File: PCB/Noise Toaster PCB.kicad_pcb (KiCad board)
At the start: 2 copper layers, 132.1 x 68.6 mm, 140 parts, among them Q1 2N5457, Q10 2N3906, Q2 2N3904, Q3 2N3904, Q4 2N3904, Q5 2N3904, Q6 2N3904, Q7 2N5457, Q8 2N5457, Q9 2N5457, U1 LM324, U2 LM324, U3 LM386

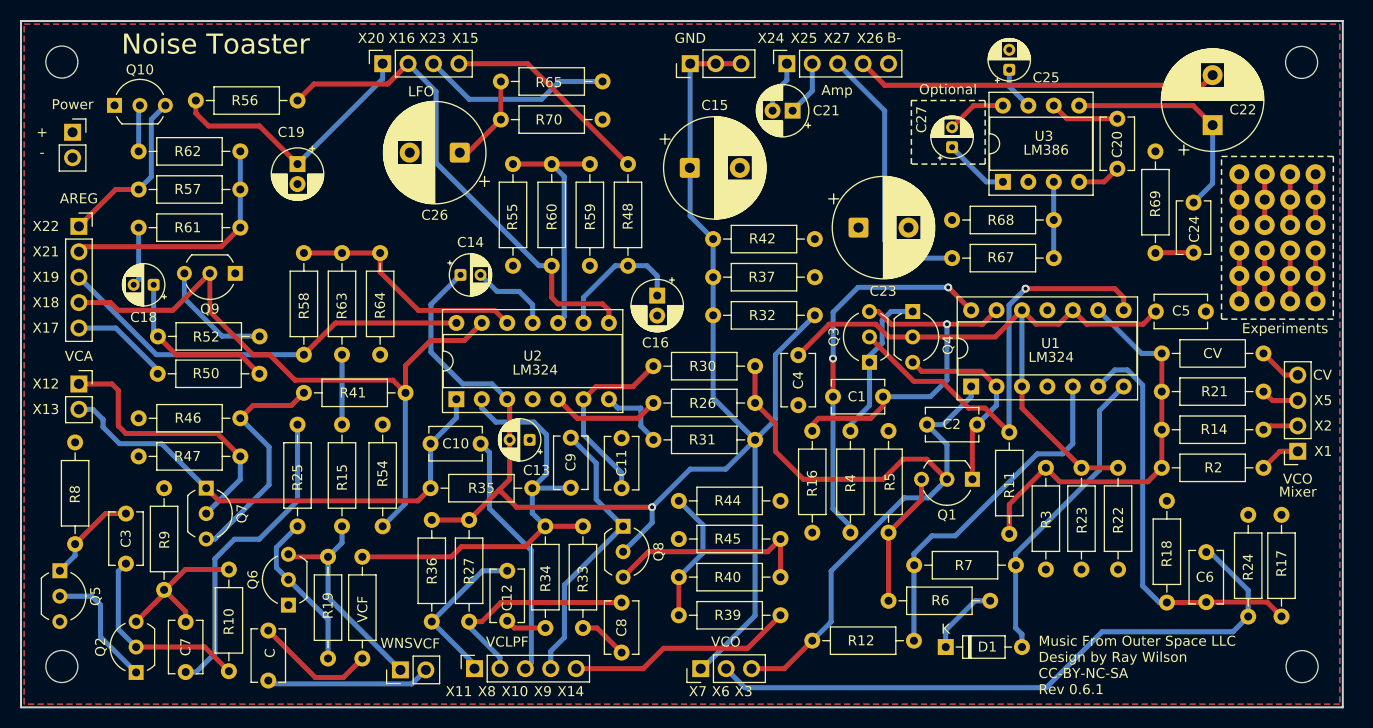
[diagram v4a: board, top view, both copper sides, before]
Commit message: Move footprints to allow mininum 20 mils distance between courtyards
except for the Q3 Q4 transistor pair
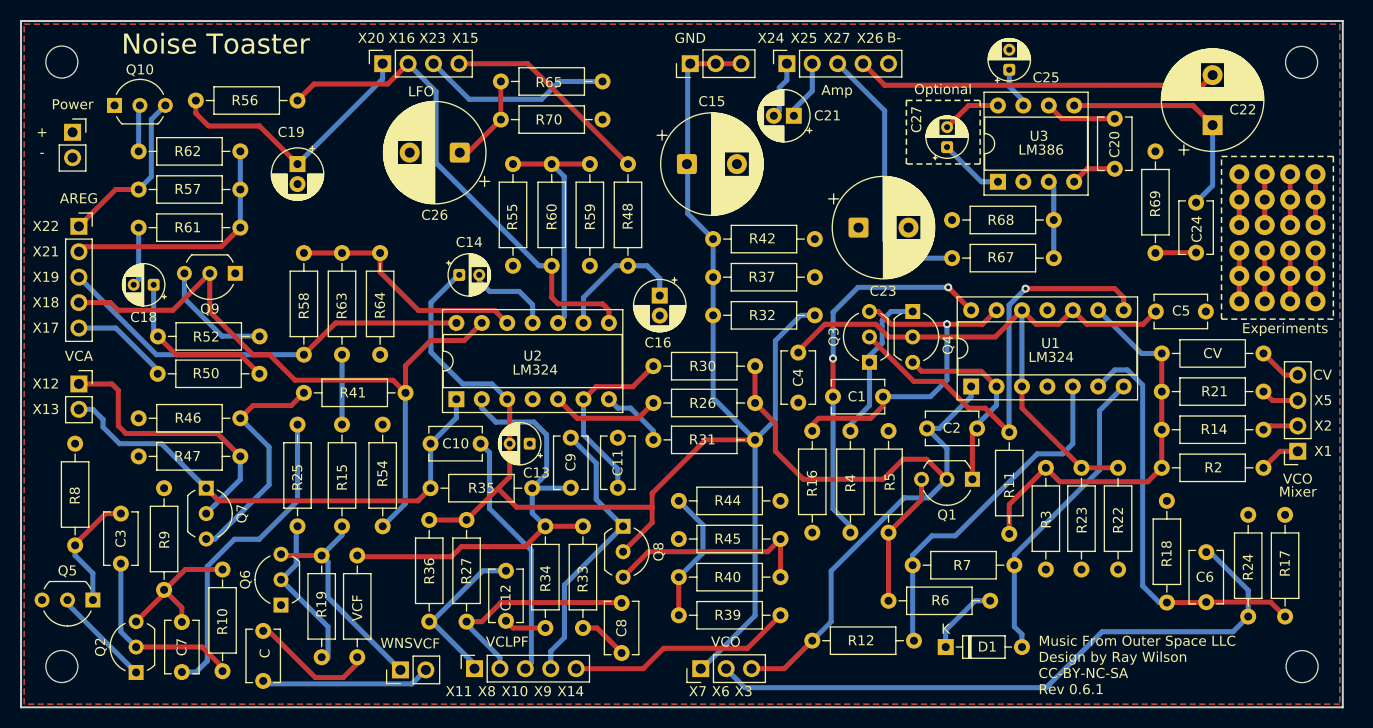
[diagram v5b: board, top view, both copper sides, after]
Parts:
- moved Q5 4.41 mm to (82.5, 133.1), turned to 180 degrees
- moved Q6 0.74 mm to (101.2, 133.6)
- moved R19 0.65 mm to (105.3, 128.7)
- moved R10 0.64 mm to (95.4, 130.1)
- moved C21 0.52 mm to (152.5, 84.7)
- moved VCF 0.52 mm to (108.9, 138.8)
- moved C 0.51 mm to (99.5, 136.2)
- moved C3 0.51 mm to (85.2, 124.5)
- moved C27 0.50 mm to (167.8, 87.9)
- moved U3 0.50 mm to (172.9, 91.3)
- moved C15 0.48 mm to (141.8, 89.6)
- moved C11 0.38 mm to (134.9, 116.9)
- moved C13 0.38 mm to (126.1, 117.5)
- moved C2 0.38 mm to (170.8, 116.0)
- moved C7 0.38 mm to (91.3, 135.3)
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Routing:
- net Net-(Q5-E): track 9.64 -> 12.0 mm
- net B-: track 31.2 -> 28.9 mm
- net GND: track 155.8 -> 157.4 mm, vias 1 -> 0
- net Net-(Q2-B): track 19.7 -> 18.4 mm
- net Net-(Q2-C): track 15.4 -> 14.6 mm
- net /WNS: track 21.6 -> 22.4 mm
- net Net-(U3-BYPASS): track 4.37 -> 3.66 mm
- net /Front Panel/X8: track 21.5 -> 22.1 mm
- net Net-(Q6-B): track 16.2 -> 15.7 mm

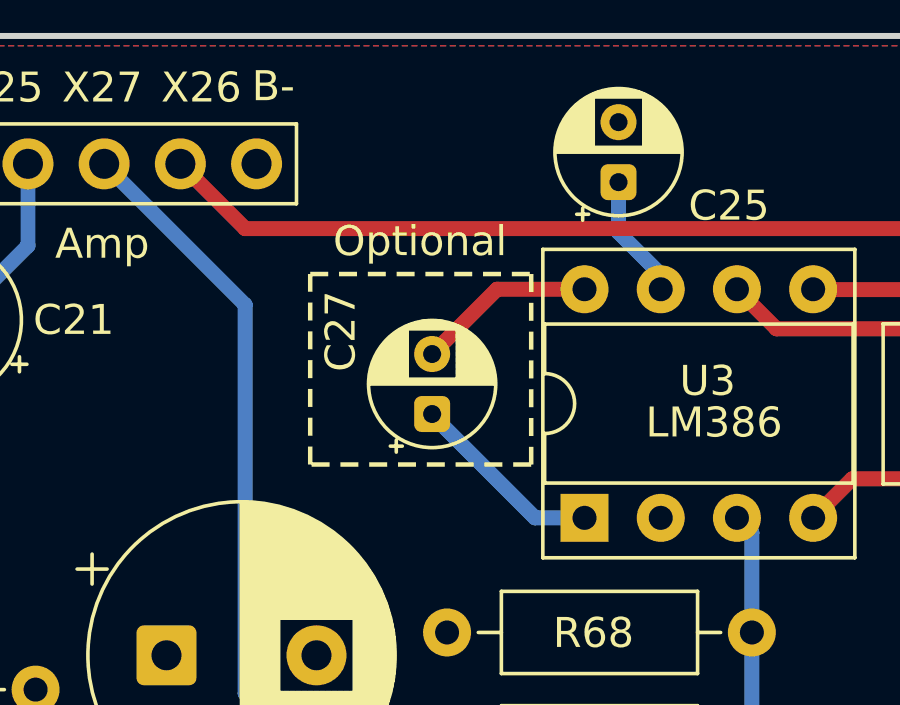
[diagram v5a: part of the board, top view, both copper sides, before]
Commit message: Added Holes for Gain Control
If you add the 10uF cap to the amplifier, you can control it by adding a potentiometer between it and pin 1
Following the internal gain equation, 30k/(150+R), you get 200 with no resistor and 20 with a 1350 ohm resistor
Choosing a 1k pot will leave you with a gain of 26 (28db) and a 1.5k equal to 18 gain (25db), albeit with some clipping
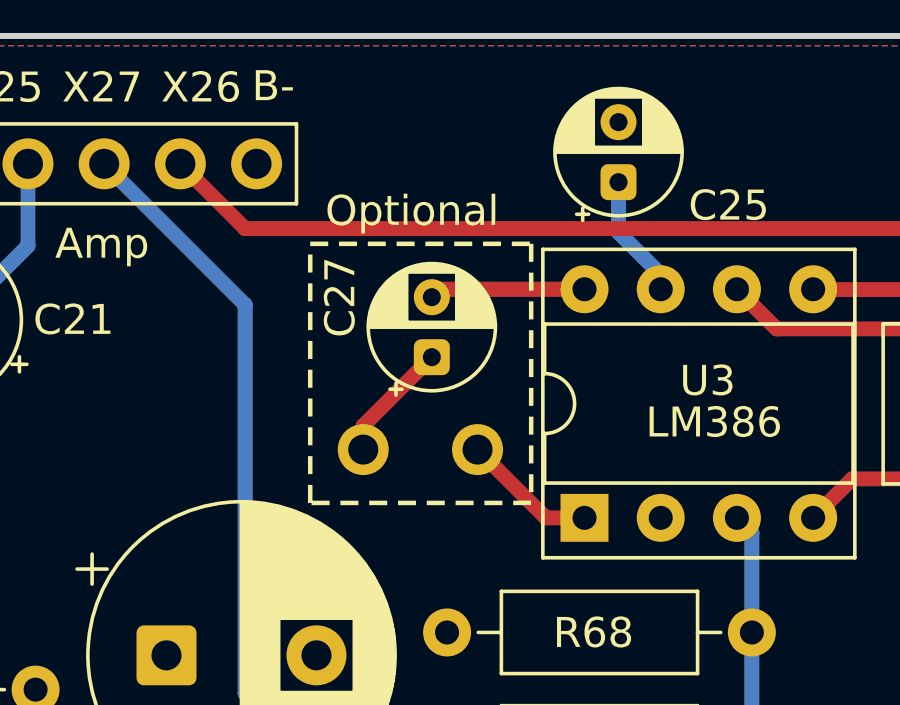
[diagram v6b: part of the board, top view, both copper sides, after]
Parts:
- added ?: , , F.Cu at (169.3, 89.1)
- added ?: , , F.Cu at (165.5, 89.1)
- moved C27 1.90 mm to (167.8, 86.0)
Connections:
- U3 pad 1: Net-(C27-Pad1) -> (no net)
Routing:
- net (no net): track 73.5 -> 78.0 mm
- net Net-(C27-Pad1): track 6.50 -> 4.03 mm
- net Net-(C27-Pad2): track 5.97 -> 5.20 mm
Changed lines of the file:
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@@
 		(capping no)
 		(filling no)
-		(zone_defaults)
 		(aux_axis_origin 75.271 143.847)
 		(grid_origin 12.096 12.092)
@@
 			(layers "*.Cu" "*.Mask")
 			(remove_unused_layers no)
-			(net "Net-(C27-Pad1)")
 			(pinfunction "GAIN")
 			(pintype "input")
@@
 		)
 	)
+	(footprint ""
+		(layer "F.Cu")
+		(at 169.322 89.054)
+		(property "Reference" ""
+			(at 0 0 0)
+			(layer "F.SilkS")
+			(effects
+				(font
+					(size 1.27 1.27)
+				)
+			)
+		)
+		(property "Value" ""
+			(at 0 0 0)
+			(layer "F.Fab")
+			(effects
+				(font
+					(size 1.27 1.27)
+				)
+			)
+		)
+		(property "Datasheet" ""
+			(at 0 0 0)
+			(layer "F.Fab")
+			(hide yes)
+			(effects
+				(font
+					(size 1.27 1.27)
+				)
+			)
+		)
+		(property "Description" ""
+			(at 0 0 0)
+			(layer "F.Fab")
+			(hide yes)
+			(effects
+				(font
+					(size 1.27 1.27)
+				)
+			)
+		)
+		(duplicate_pad_numbers_are_jumpers no)
+		(pad "1" thru_hole circle
+			(at 0 0 90)
+			(size 1.7 1.7)
+			(drill 1)
+			(layers "*.Cu" "*.Mask")
+			(remove_unused_layers no)
+		)
+		(embedded_fonts no)
+	)
 	(footprint "Capacitor_THT:C_Disc_D5.1mm_W3.2mm_P5.00mm"
 		(layer "F.Cu")
@@
 		)
 	)
+	(footprint ""
+		(layer "F.Cu")
+		(at 165.512 89.054)
+		(property "Reference" ""
+			(at 0 0 0)
+			(layer "F.SilkS")
+			(effects
+				(font
+					(size 1.27 1.27)
+				)
+			)
+		)
+		(property "Value" ""
+			(at 0 0 0)
+			(layer "F.Fab")
+			(effects
+				(font
+					(size 1.27 1.27)
+				)
+			)
+		)
+		(property "Datasheet" ""
+			(at 0 0 0)
+			(layer "F.Fab")
+			(hide yes)
+			(effects
+				(font
+					(size 1.27 1.27)
+				)
+			)
+		)
+		(property "Description" ""
+			(at 0 0 0)
+			(layer "F.Fab")
+			(hide yes)
+			(effects
+				(font
+					(size 1.27 1.27)
+				)
+			)
+		)
+		(duplicate_pad_numbers_are_jumpers no)
+		(pad "1" thru_hole circle
+			(at 0 0 90)
+			(size 1.7 1.7)
+			(drill 1)
+			(layers "*.Cu" "*.Mask")
+			(remove_unused_layers no)
+			(net "Net-(C27-Pad1)")
+		)
+		(embedded_fonts no)
+	)
 	(footprint "Resistor_THT:R_Axial_DIN0207_L6.3mm_D2.5mm_P10.16mm_Horizontal"
 		(layer "F.Cu")
@@
 	(footprint "Capacitor_THT:CP_Radial_D4.0mm_P2.00mm"
 		(layer "F.Cu")
-		(at 167.808 87.869 90)
+		(at 167.798 85.974 90)
 		(descr "CP, Radial series, Radial, pin pitch=2.00mm, diameter=4mm, height=7mm, Electrolytic Capacitor")
 		(tags "CP Radial series Radial pin pitch 2.00mm diameter 4mm height 7mm Electrolytic Capacitor")
 		(property "Reference" "C27"
-			(at 2.762 -3.048 90)
+			(at 2 -3.048 90)
 			(layer "F.SilkS")
 			(effects
@@
 	)
 	(gr_rect
-		(start 163.744 83.202)
-		(end 171.11 89.552)
+		(start 163.744 82.196)
+		(end 171.11 90.832)
 		(stroke
 			(width 0.15)
@@
 	)
 	(gr_text "Optional"
-		(at 164.506 82.694 0)
+		(at 164.242 81.688 0)
 		(layer "F.SilkS")
 		(effects
@@
 	)
 	(segment
+		(start 172.888 91.33)
+		(end 171.598 91.33)
+		(width 0.5)
+		(layer "F.Cu")
+		(net "")
+	)
+	(segment
 		(start 104.679 140.87)
 		(end 100.02 136.211)
@@
 	)
 	(segment
+		(start 171.598 91.33)
+		(end 169.322 89.054)
+		(width 0.5)
+		(layer "F.Cu")
+		(net "")
+	)
+	(segment
 		(start 202.088 98.198)
 		(end 202.088 103.278)
@@
 	)
 	(segment
-		(start 171.237 91.33)
-		(end 172.888 91.33)
+		(start 165.512 88.26)
+		(end 167.798 85.974)
 		(width 0.5)
-		(layer "B.Cu")
+		(layer "F.Cu")
 		(net "Net-(C27-Pad1)")
 	)
 	(segment
-		(start 167.808 87.901)
-		(end 171.237 91.33)
+		(start 165.512 89.054)
+		(end 165.512 88.26)
 		(width 0.5)
-		(layer "B.Cu")
+		(layer "F.Cu")
 		(net "Net-(C27-Pad1)")
 	)
@@
 	)
 	(segment
-		(start 172.888 83.71)
-		(end 169.967 83.71)
+		(start 168.062 83.71)
+		(end 167.798 83.974)
 		(width 0.5)
 		(layer "F.Cu")
@@
 	)
 	(segment
-		(start 169.967 83.71)
-		(end 167.808 85.869)
+		(start 172.888 83.71)
+		(end 168.062 83.71)
 		(width 0.5)
 		(layer "F.Cu")

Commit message: Necessary Changes to Schematic and PCB
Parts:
- removed Amp: Amp, Connector_PinSocket_2.54mm:PinSocket_1x05_P2.54mm_Vertical
- removed C: 0.1 uF, Capacitor_THT:C_Disc_D5.1mm_W3.2mm_P5.00mm
- removed CV: R_Axial_DIN0207_L6.3mm_D2.5mm_P10.16mm_Horizontal, Resistor_THT:R_Axial_DIN0207_L6.3mm_D2.5mm_P10.16mm_Horizontal
- removed VCF: 3 M, Resistor_THT:R_Axial_DIN0207_L6.3mm_D2.5mm_P10.16mm_Horizontal
- removed VCLPF: VCLPF, Connector_PinSocket_2.54mm:PinSocket_1x05_P2.54mm_Vertical
- added C28: 100nF, Capacitor_THT:C_Disc_D5.1mm_W3.2mm_P5.00mm, F.Cu at (100.7, 141.6)
- added CV1: 100k, Resistor_THT:R_Axial_DIN0207_L6.3mm_D2.5mm_P10.16mm_Horizontal, F.Cu at (189.1, 108.4)
- added J7: LPF, Connector_PinSocket_2.54mm:PinSocket_1x06_P2.54mm_Vertical, F.Cu at (118.0, 139.9)
- added J9: Amp, Connector_PinSocket_2.54mm:PinSocket_1x05_P2.54mm_Vertical, F.Cu at (151.8, 79.4)
- added VCF1: 3 M, Resistor_THT:R_Axial_DIN0207_L6.3mm_D2.5mm_P10.16mm_Horizontal, F.Cu at (108.9, 128.7)
- C10, C9: value 0.001 uF -> 1nF
- C11, C12, C20, C3, C4, C5, C7, C8: value 0.1 uF -> 100nF
- C16, C19, C21: value 1 uF -> 1uF
- C18: value 4.7 uF -> 4u7F
- C24: value 0.047 uF -> 47nF
- C25: value 10 uF -> 10uF
- C26: value 470 uF -> 470uF
- C6: value 0.01 uF -> 10nF
- J10: renamed from GND; footprint Connector_PinHeader_2.54mm:PinHeader_1x03_P2.54mm_Vertical -> Connector_PinSocket_2.54mm:PinSocket_1x04_P2.54mm_Vertical
- J6: renamed from VCO; footprint Connector_PinHeader_2.54mm:PinHeader_1x03_P2.54mm_Vertical -> Connector_PinSocket_2.54mm:PinSocket_1x03_P2.54mm_Vertical
- R11: value 2 K -> 2k
- R14, R55, R58, R59, R60: value 100 K -> 100k
- R16: value 2 M -> 2M
- R2: value 75 K -> 75k
- R21: value 36 K -> 36k
- R22, R23: value 4.7 K -> 4k7
- R3: value 270 K -> 270k
- R33, R35: value 4.7 M -> 4M7
- R37, R42: value 4.7 k -> 4k7
- R4, R52, R61, R62: value 10 K -> 10k
- R48, R65, R70: value 3 K -> 3k
- R50: value 820 Ohm -> 820
- R54: value 4,7 K -> 4k7
- R56: value 20 K -> 20k
- R57: value 200 Ohm -> 200
- R63, R64: value 150 K -> 150k
- R69: value 10 Ohm -> 10
- X4: renamed from WNS; footprint Connector_PinHeader_2.54mm:PinHeader_1x02_P2.54mm_Vertical -> Connector_PinSocket_2.54mm:PinSocket_1x01_P2.54mm_Vertical
- moved C4 32.8 mm to (184.6, 99.7), turned to 90 degrees
- moved J10 2.80 mm to (139.3, 79.4)
- moved C14 0.48 mm to (119.1, 101.1)
- moved C12 0.33 mm to (123.7, 130.5)
- moved X4 0.25 mm to (113.2, 139.9)
- moved C2 0.13 mm to (170.7, 116.0)
- moved R14 0.13 mm to (189.1, 116.1)
- moved R2 0.13 mm to (189.1, 119.9)
- moved R21 0.13 mm to (189.1, 112.3)
- moved J4 0.13 mm to (111.4, 79.4)
- moved J6 0.13 mm to (143.2, 139.9)
- moved R33 0.06 mm to (131.5, 135.9)
- renumbered Power to J2, AREG to J3, LFO to J4, VCO to J5, VCA to J8
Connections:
- J5 pad 4: (no net) -> Net-(J5-Pin_4)
- J6 pad 1: GND -> /SQR
- R31 pad 2: GND -> /SQR
- R32 pad 2: GND -> /SQR
- U3 pad 1: (no net) -> Net-(C27-Pad1)
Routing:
- net GND: track 157.4 -> 113.0 mm
- net /SQR: track 0.00 -> 40.7 mm
- net (no net): track 78.0 -> 40.6 mm
- net Net-(J7-Pin_1): track 0.00 -> 18.4 mm
- net Net-(C28-Pad1): track 0.00 -> 9.27 mm
- net B-: track 28.9 -> 20.2 mm
- net /G2: track 62.6 -> 55.8 mm
- net Net-(C27-Pad1): track 4.03 -> 8.54 mm
- net Net-(J5-Pin_4): track 0.00 -> 4.50 mm
- net /FO: track 49.8 -> 53.5 mm
- net /RMP: track 72.3 -> 69.5 mm
- net /Front Panel/X14: track 22.5 -> 23.4 mm
- net /WNS: track 22.4 -> 21.6 mm
- net /Audio Amplifier/X24: track 5.75 -> 6.38 mm
- net /Front Panel/X10: track 24.8 -> 24.2 mm
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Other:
- board text removed: "VCF"
